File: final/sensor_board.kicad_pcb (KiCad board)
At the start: 2 copper layers, 50 x 30 mm, 77 parts, among them J1 USB_microB_2040002-1, J2 Arduino_ICSP, J3 Conn_01x02_Male, J4 Conn_01x15_Male, J5 Conn_01x15_Male, J6 BT CONFIG, SW1 SW_DIP_x01, U1 NC7SZ04P5X, U10 BQ24075, U11 BQ27441-G1, U2 MCP1702T-3302E/CBCT-ND, U3 TXS0104E, U4 TPS61200DRC, U5 FT232RL, U6 RN4871, U7 TPS2113ADRBR, U8 US5881, U9 ATMEGA328PB-ANR, Y1 16MHz

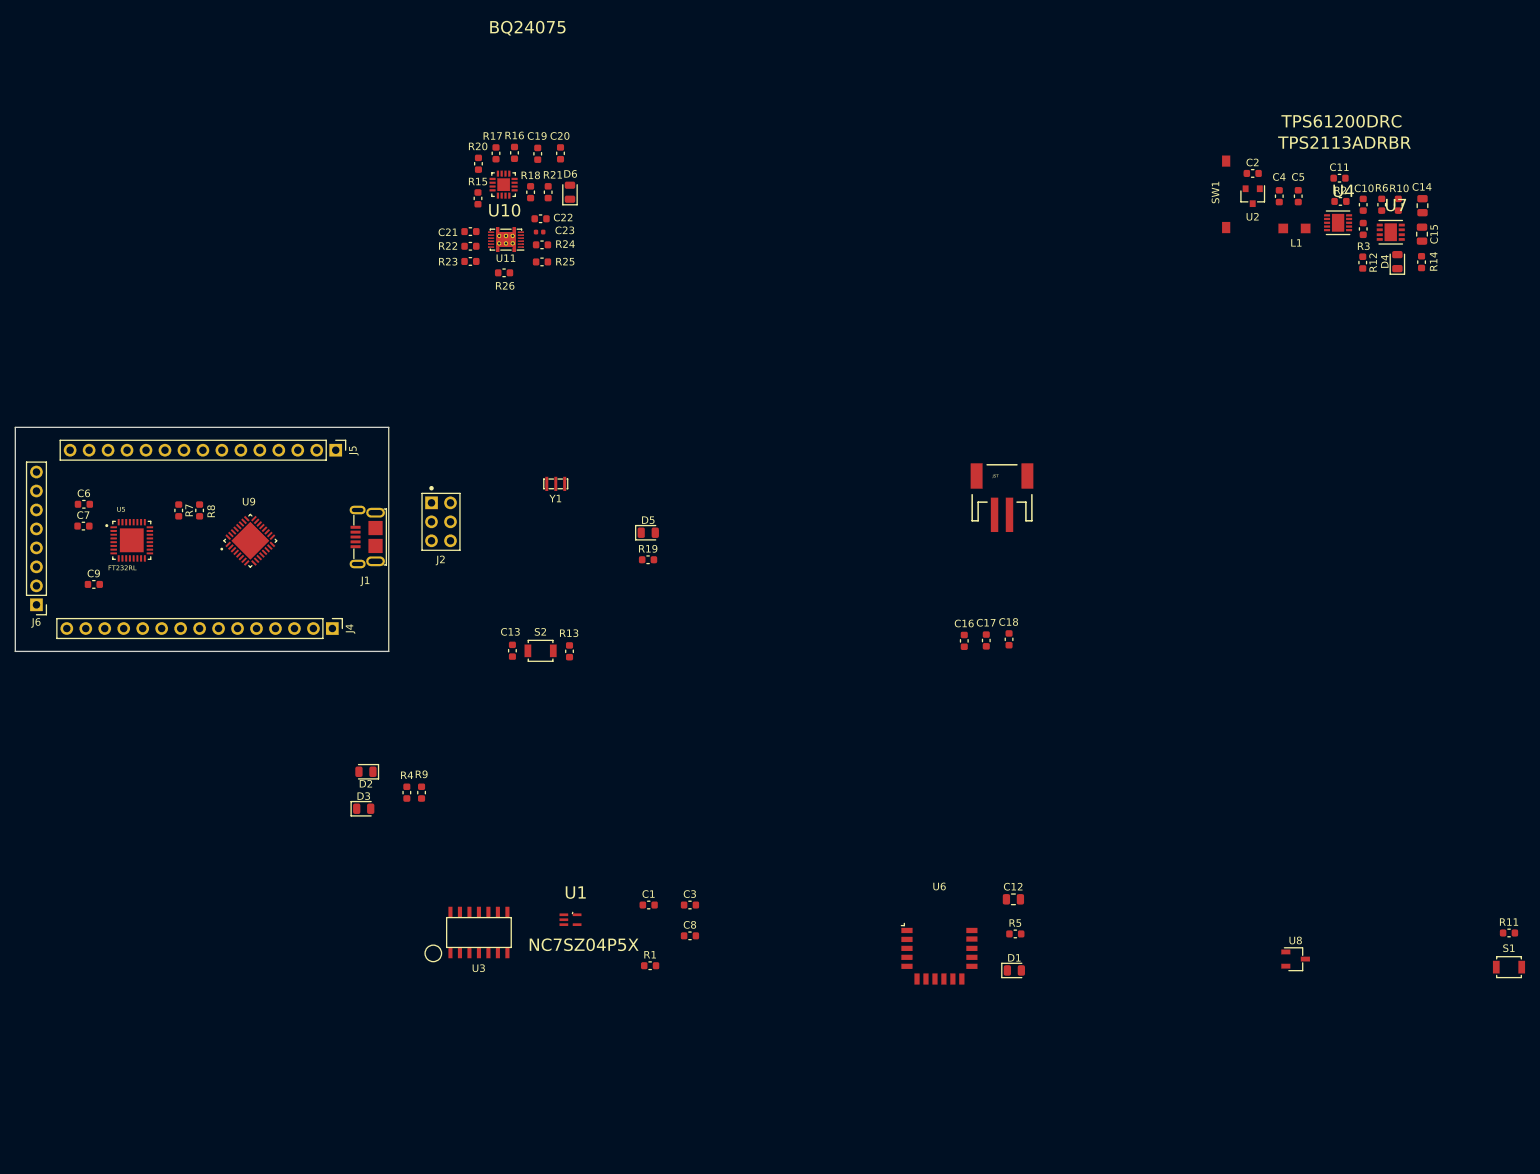
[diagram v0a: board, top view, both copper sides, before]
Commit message: sensor board layout updates
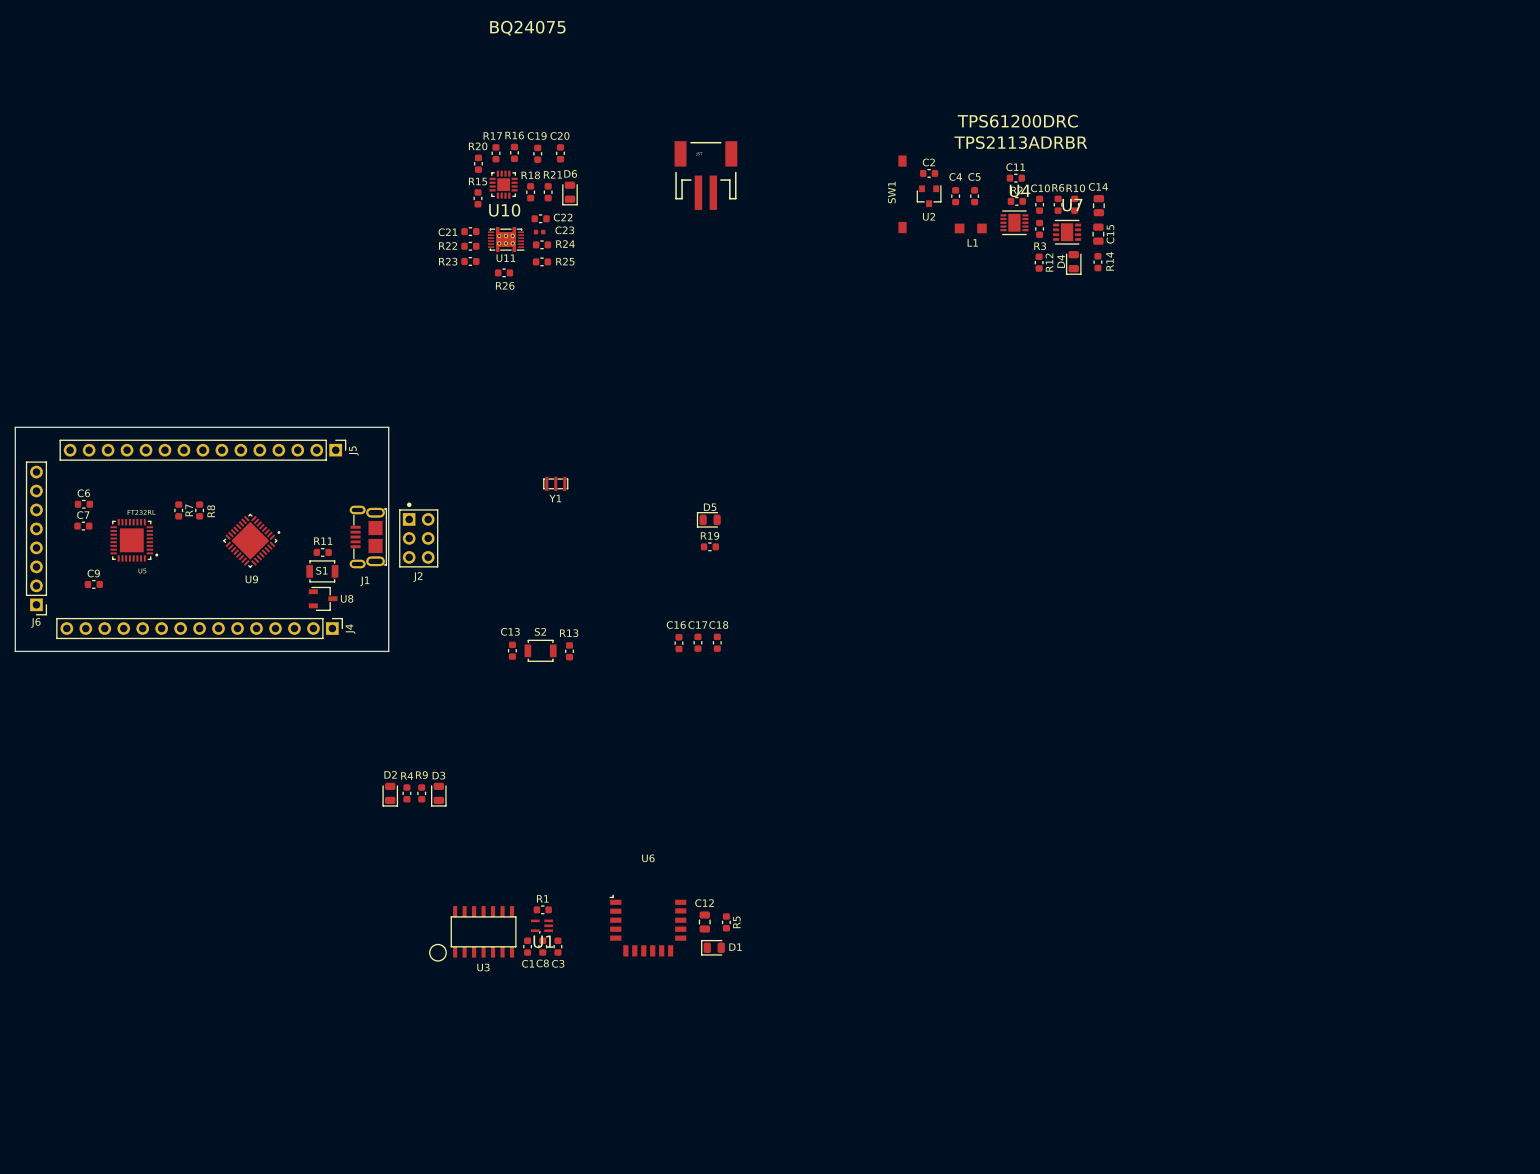
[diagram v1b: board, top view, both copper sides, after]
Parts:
- moved S1 167.5 mm to (90.7, 59.0), turned to 180 degrees
- moved R11 166.8 mm to (90.8, 56.5), turned to 180 degrees
- moved U8 138.9 mm to (90.8, 62.7)
- moved J3 58.6 mm to (142.1, 4.62)
- moved C10 43.3 mm to (186.8, 9.93)
- moved C11 43.3 mm to (183.6, 6.38)
- moved C14 43.3 mm to (194.7, 10.1)
- moved C15 43.3 mm to (194.6, 13.9)
- moved C2 43.3 mm to (172.0, 5.74)
- moved C4 43.3 mm to (175.5, 8.79)
- moved C5 43.3 mm to (178.1, 8.79)
- moved D4 43.3 mm to (191.3, 17.6)
- moved L1 43.3 mm to (177.6, 13.1)
- moved R12 43.3 mm to (186.7, 17.7)
- moved R14 43.3 mm to (194.6, 17.6)
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
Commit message: sensor board layout progress
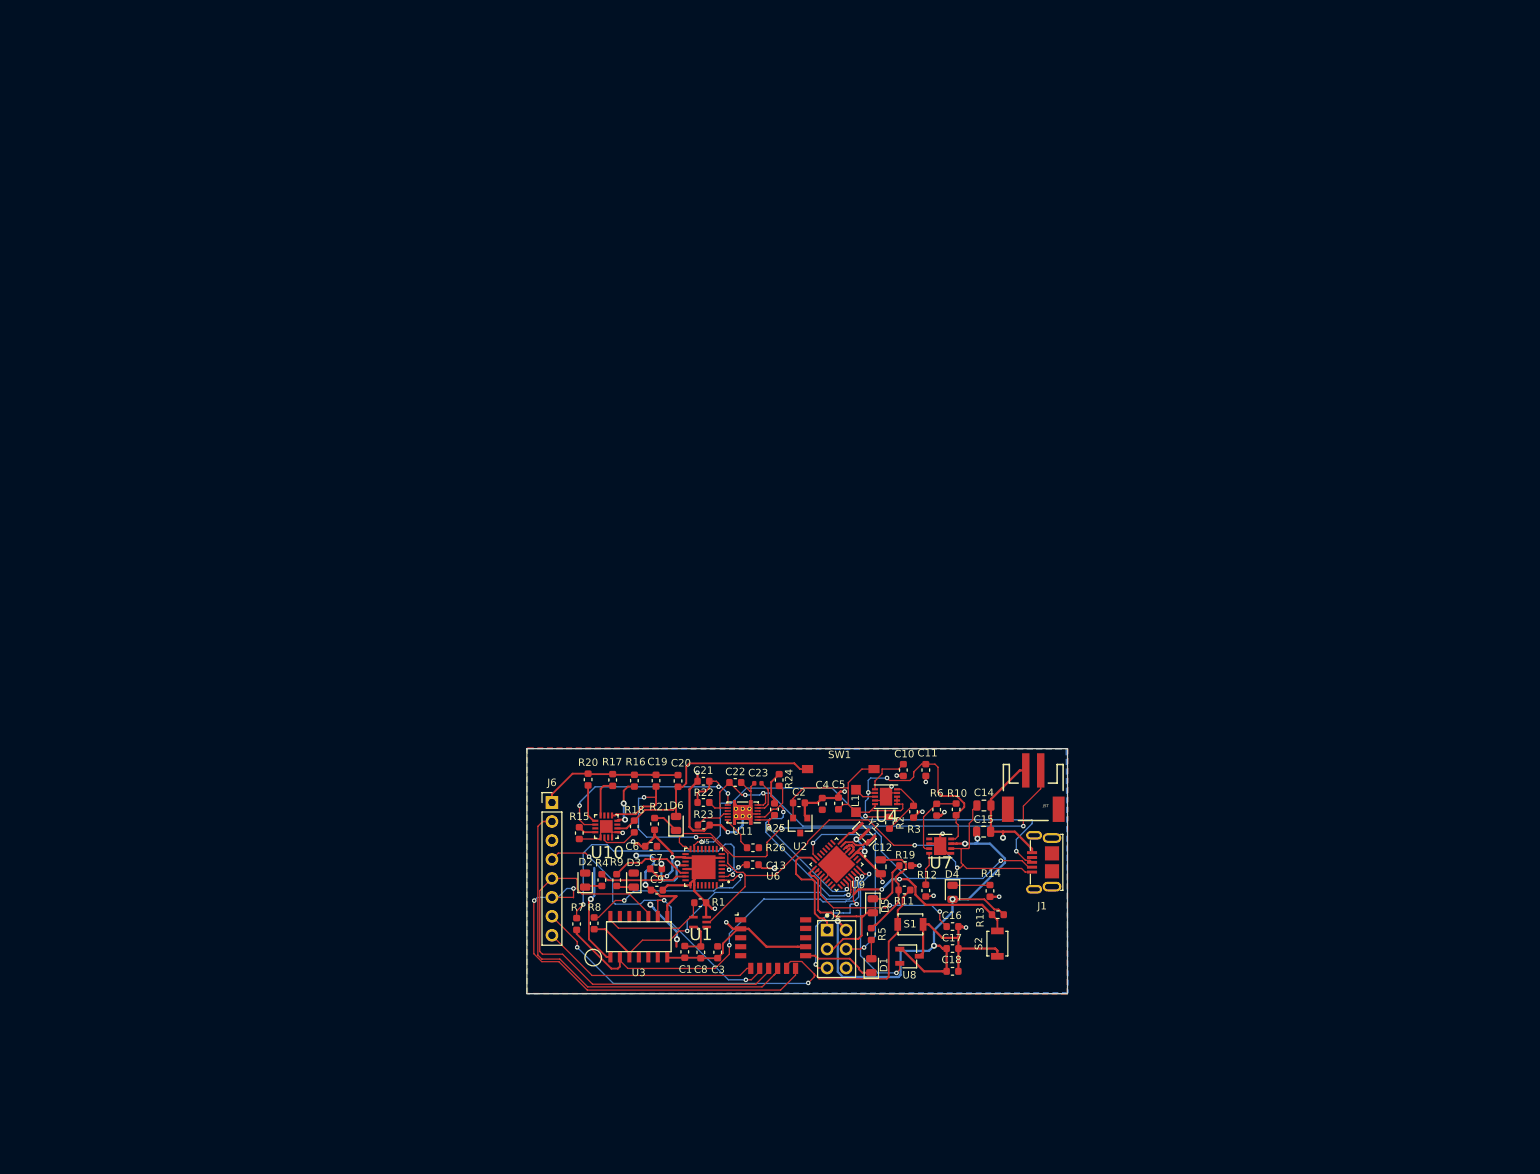
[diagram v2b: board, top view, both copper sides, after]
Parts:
- removed J4, J5: Conn_01x15_Male, Connector_PinHeader_2.54mm:PinHeader_1x15_P2.54mm_Vertical
- moved J1 100.5 mm to (188.4, 98.0)
- moved J3 95.4 mm to (185.9, 89.4), turned to 180 degrees
- moved U8 92.0 mm to (169.4, 110.6)
- moved S1 91.8 mm to (169.5, 106.3)
- moved R11 90.1 mm to (168.7, 101.7), turned to 0 degrees
- moved U9 89.7 mm to (159.6, 98.3)
- moved C7 89.4 mm to (135.4, 98.8)
- moved C6 88.7 mm to (134.7, 95.8)
- moved U5 88.2 mm to (141.8, 98.6)
- moved U10 87.0 mm to (128.8, 93.2)
- moved R15 86.1 mm to (125.1, 94.1)
- moved C2 86.1 mm to (154.5, 90.0)
- moved R18 86.1 mm to (132.5, 93.2)
- moved U2 86.0 mm to (154.7, 93.1)
- moved D4 86.0 mm to (175.1, 102.0), turned to 270 degrees
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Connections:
- U5 pad 33: (no net) -> GND
- U9 pad 33: (no net) -> GND
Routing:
- net GND: track 0.00 -> 208.0 mm, vias 0 -> 23
- net +5V: track 0.00 -> 101.6 mm, vias 0 -> 8
- net /UART_EN: track 0.00 -> 97.7 mm, vias 0 -> 4
- net /~RST: track 0.00 -> 68.2 mm, vias 0 -> 2
- net Net-(J1-Pad3): track 0.00 -> 61.1 mm, vias 0 -> 2
- net /TX: track 0.00 -> 60.1 mm
- net /BATTERY: track 0.00 -> 59.8 mm, vias 0 -> 3
- net Net-(J1-Pad2): track 0.00 -> 59.2 mm, vias 0 -> 2
- net /RTS: track 0.00 -> 56.6 mm
- net /CTS: track 0.00 -> 56.0 mm, vias 0 -> 2
- net /D1: track 0.00 -> 53.2 mm, vias 0 -> 2
- net /RESET: track 0.00 -> 45.2 mm, vias 0 -> 5
- net /D0: track 0.00 -> 44.7 mm, vias 0 -> 2
- net /RX: track 0.00 -> 42.5 mm, vias 0 -> 3
- net Net-(R7-Pad1): track 0.00 -> 35.5 mm, vias 0 -> 2
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- added copper zone on F.Cu, net +3V3
- added copper zone on B.Cu, net GND
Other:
- board size 50 x 30 mm -> 72.4 x 32.8 mm
- net class Default: clearance 0.2 -> 0.1
- rule trace_clearance: 0.2 -> 0.1
- rule trace_min: 0.2 -> 0.1524
- rule via_min_size: 0.4 -> 0.6096

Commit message: merge conflict resolved
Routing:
- net +3V3: track 34.7 -> 41.8 mm, vias 2 -> 4
- net (no net): track 7.13 -> 0.00 mm, vias 2 -> 0
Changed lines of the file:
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@@
   )
   (setup
-    (last_trace_width 0.3048)
+    (last_trace_width 0.25)
     (user_trace_width 0.1524)
     (user_trace_width 0.254)
@@
   (gr_line (start 190.5 82.75828) (end 190.5 115.57) (layer Edge.Cuts) (width 0.1))
   (gr_line (start 118.11 82.75828) (end 190.5 82.75828) (layer Edge.Cuts) (width 0.1))
-  (via (at 138.209466 108.288266) (size 0.8) (drill 0.4) (layers F.Cu B.Cu) (net 0))
-  (segment (start 138.14552 108.352212) (end 138.209466 108.288266) (width 0.3048) (layer F.Cu) (net 0))
-  (segment (start 138.14552 109.2708) (end 138.14552 108.352212) (width 0.3048) (layer F.Cu) (net 0))
-  (segment (start 138.209466 107.28487) (end 135.128 104.203404) (width 0.3048) (layer B.Cu) (net 0))
-  (segment (start 138.209466 108.288266) (end 138.209466 107.28487) (width 0.3048) (layer B.Cu) (net 0))
-  (via (at 134.65048 103.64432) (size 0.8) (drill 0.4) (layers F.Cu B.Cu) (net 0))
-  (segment (start 135.128 104.12184) (end 134.65048 103.64432) (width 0.3048) (layer B.Cu) (net 0))
-  (segment (start 135.128 104.203404) (end 135.128 104.12184) (width 0.3048) (layer B.Cu) (net 0))
+  (via (at 138.209466 108.288266) (size 0.8) (drill 0.4) (layers F.Cu B.Cu) (net 1))
+  (segment (start 138.14552 108.352212) (end 138.209466 108.288266) (width 0.3048) (layer F.Cu) (net 1))
+  (segment (start 138.14552 109.2708) (end 138.14552 108.352212) (width 0.3048) (layer F.Cu) (net 1))
+  (segment (start 138.209466 107.28487) (end 135.128 104.203404) (width 0.3048) (layer B.Cu) (net 1))
+  (segment (start 138.209466 108.288266) (end 138.209466 107.28487) (width 0.3048) (layer B.Cu) (net 1))
+  (via (at 134.65048 103.64432) (size 0.8) (drill 0.4) (layers F.Cu B.Cu) (net 1))
+  (segment (start 135.128 104.12184) (end 134.65048 103.64432) (width 0.3048) (layer B.Cu) (net 1))
+  (segment (start 135.128 104.203404) (end 135.128 104.12184) (width 0.3048) (layer B.Cu) (net 1))
   (segment (start 139.3191 109.2454) (end 139.2555 109.1818) (width 0.25) (layer F.Cu) (net 1))
   (segment (start 141.4018 109.2454) (end 139.3191 109.2454) (width 0.25) (layer F.Cu) (net 1))

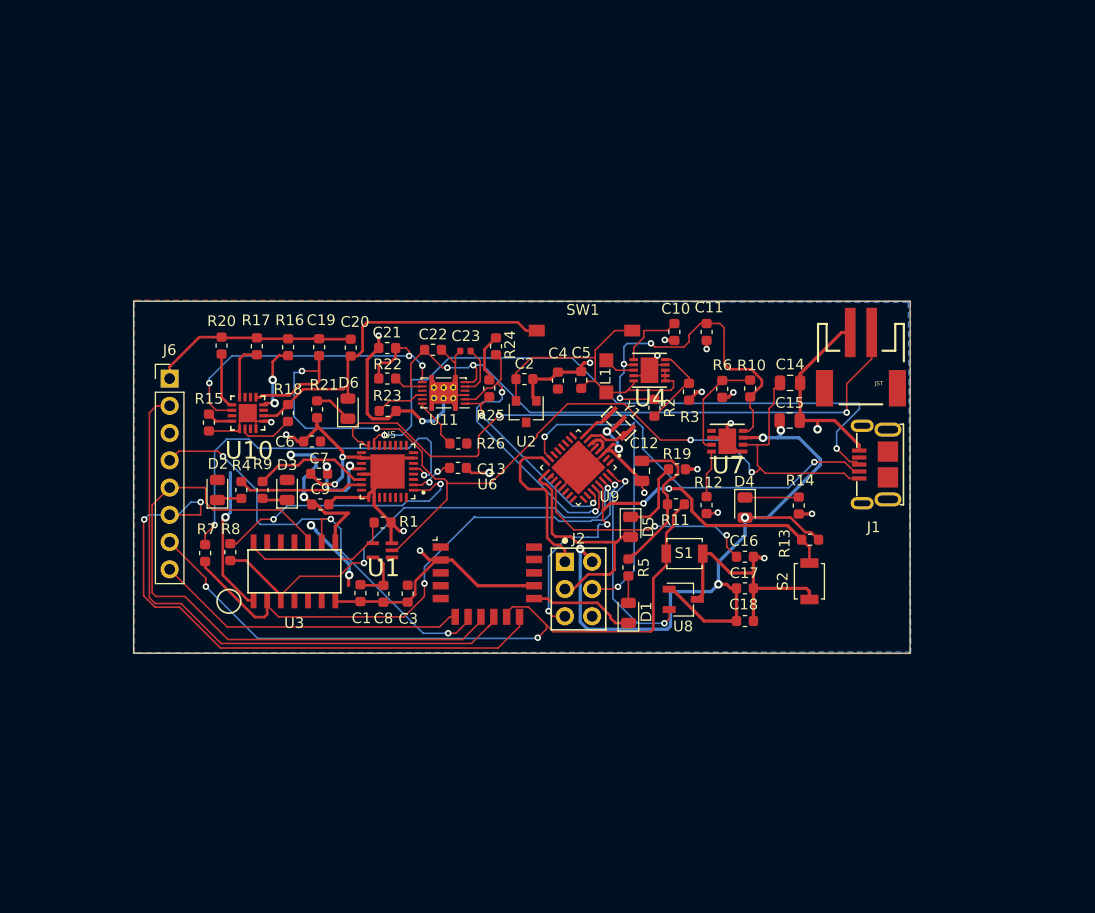
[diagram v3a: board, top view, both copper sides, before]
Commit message: changes to senor layout
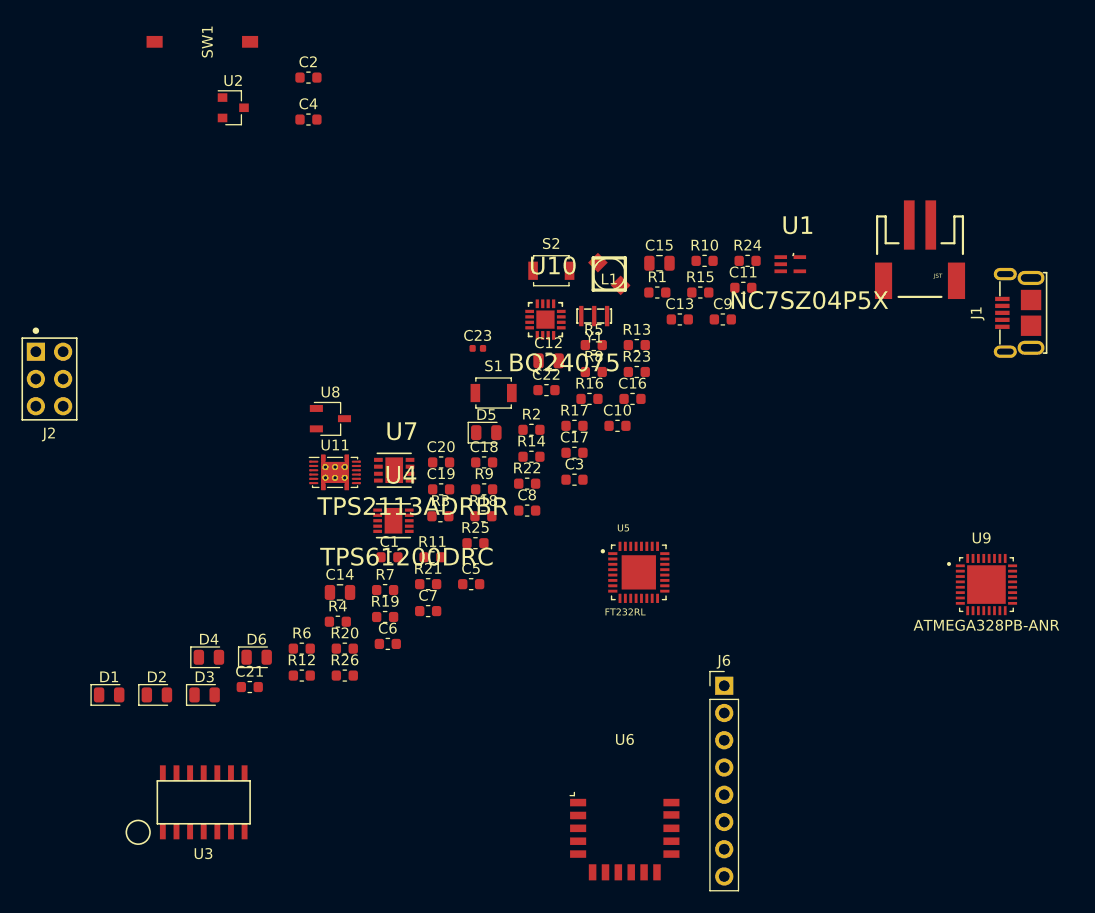
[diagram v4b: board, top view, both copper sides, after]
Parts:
- moved J6 59.1 mm to (173.2, 118.6)
- moved J2 53.1 mm to (110.3, 90.0)
- moved D4 51.9 mm to (125.1, 116.0), turned to 0 degrees
- moved D1 49.0 mm to (115.8, 119.5), turned to 0 degrees
- moved R15 47.4 mm to (170.9, 81.9), turned to 0 degrees
- moved U1 46.5 mm to (179.3, 79.3), turned to 0 degrees
- moved C14 46.3 mm to (137.4, 109.9)
- moved R6 46.1 mm to (133.8, 115.1), turned to 0 degrees
- moved SW1 44.7 mm to (124.5, 58.6), turned to 90 degrees
- moved C9 41.3 mm to (173.0, 84.5)
- moved R12 40.9 mm to (133.8, 117.7), turned to 0 degrees
- moved U9 39.6 mm to (197.6, 109.2), turned to 0 degrees
- moved U2 39.3 mm to (127.4, 64.7), turned to 0 degrees
- moved R8 37.8 mm to (161.0, 89.4), turned to 0 degrees
- moved S2 37.6 mm to (157.1, 79.9), turned to 0 degrees
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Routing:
- net GND: track 208.0 -> 0.00 mm, vias 23 -> 0
- net +5V: track 101.6 -> 0.00 mm, vias 8 -> 0
- net /UART_EN: track 97.7 -> 0.00 mm, vias 4 -> 0
- net /~RST: track 68.2 -> 0.00 mm, vias 2 -> 0
- net Net-(J1-Pad3): track 61.1 -> 0.00 mm, vias 2 -> 0
- net /TX: track 60.1 -> 0.00 mm
- net /BATTERY: track 59.8 -> 0.00 mm, vias 3 -> 0
- net Net-(J1-Pad2): track 59.2 -> 0.00 mm, vias 2 -> 0
- net /RTS: track 56.6 -> 0.00 mm
- net /CTS: track 56.0 -> 0.00 mm, vias 2 -> 0
- net /D1: track 53.2 -> 0.00 mm, vias 2 -> 0
- net /RESET: track 45.2 -> 0.00 mm, vias 5 -> 0
- net /D0: track 44.7 -> 0.00 mm, vias 2 -> 0
- net /RX: track 42.5 -> 0.00 mm, vias 3 -> 0
- net +3V3: track 41.8 -> 0.00 mm, vias 4 -> 0
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- removed copper zone on F.Cu, net +3V3
- removed copper zone on B.Cu, net GND
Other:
- board outline removed
- net class Default: clearance 0.1 -> 0.2
- rule trace_clearance: 0.1 -> 0.2
